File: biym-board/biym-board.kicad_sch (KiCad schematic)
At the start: 1 part

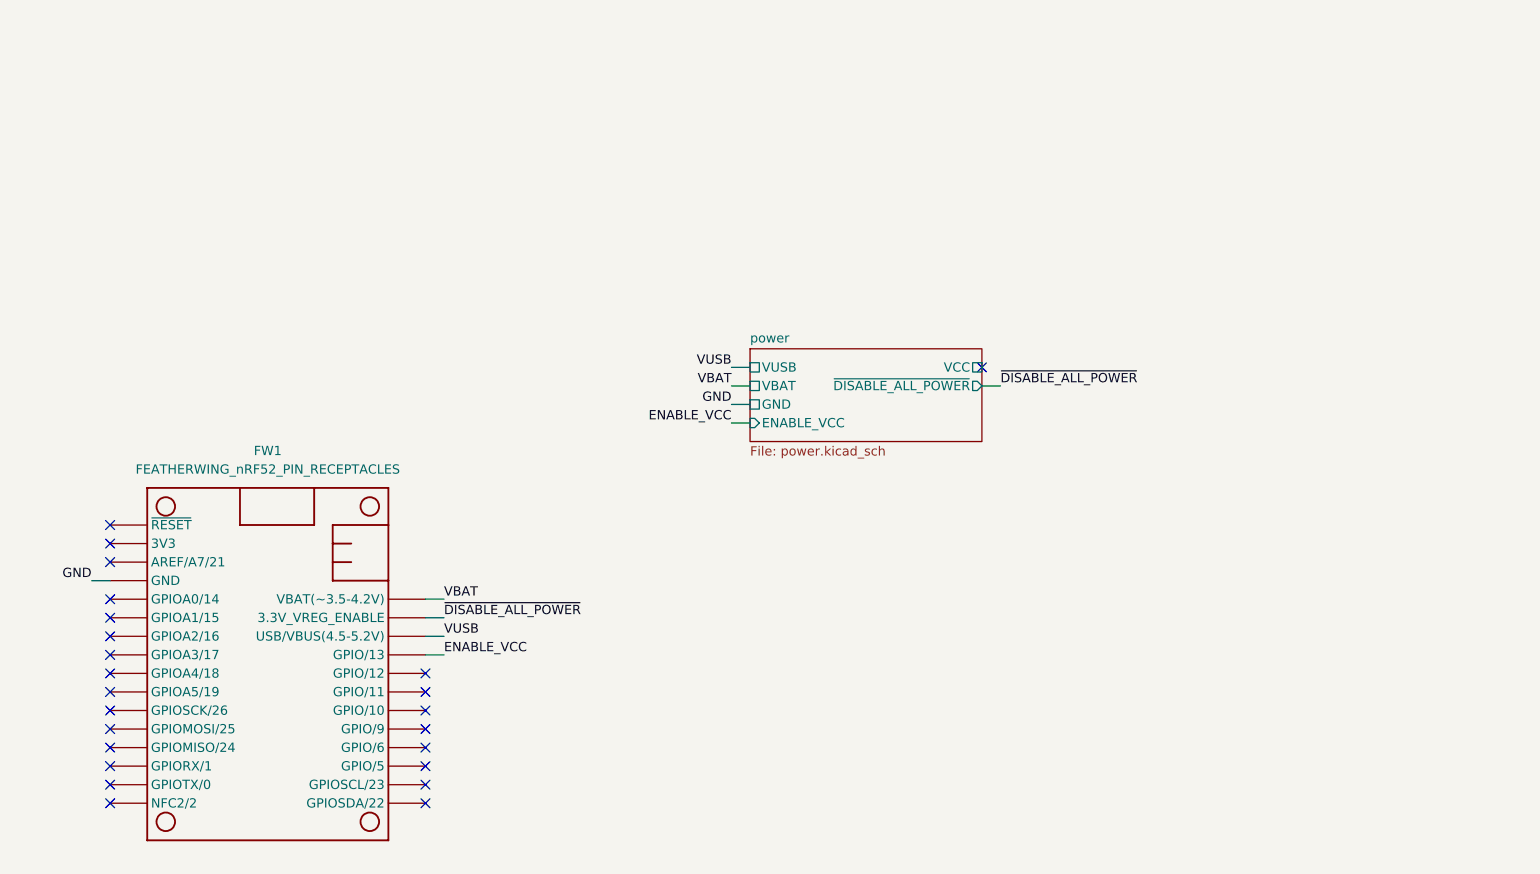
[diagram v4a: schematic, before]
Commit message: Switch feather contacts to pogo pins
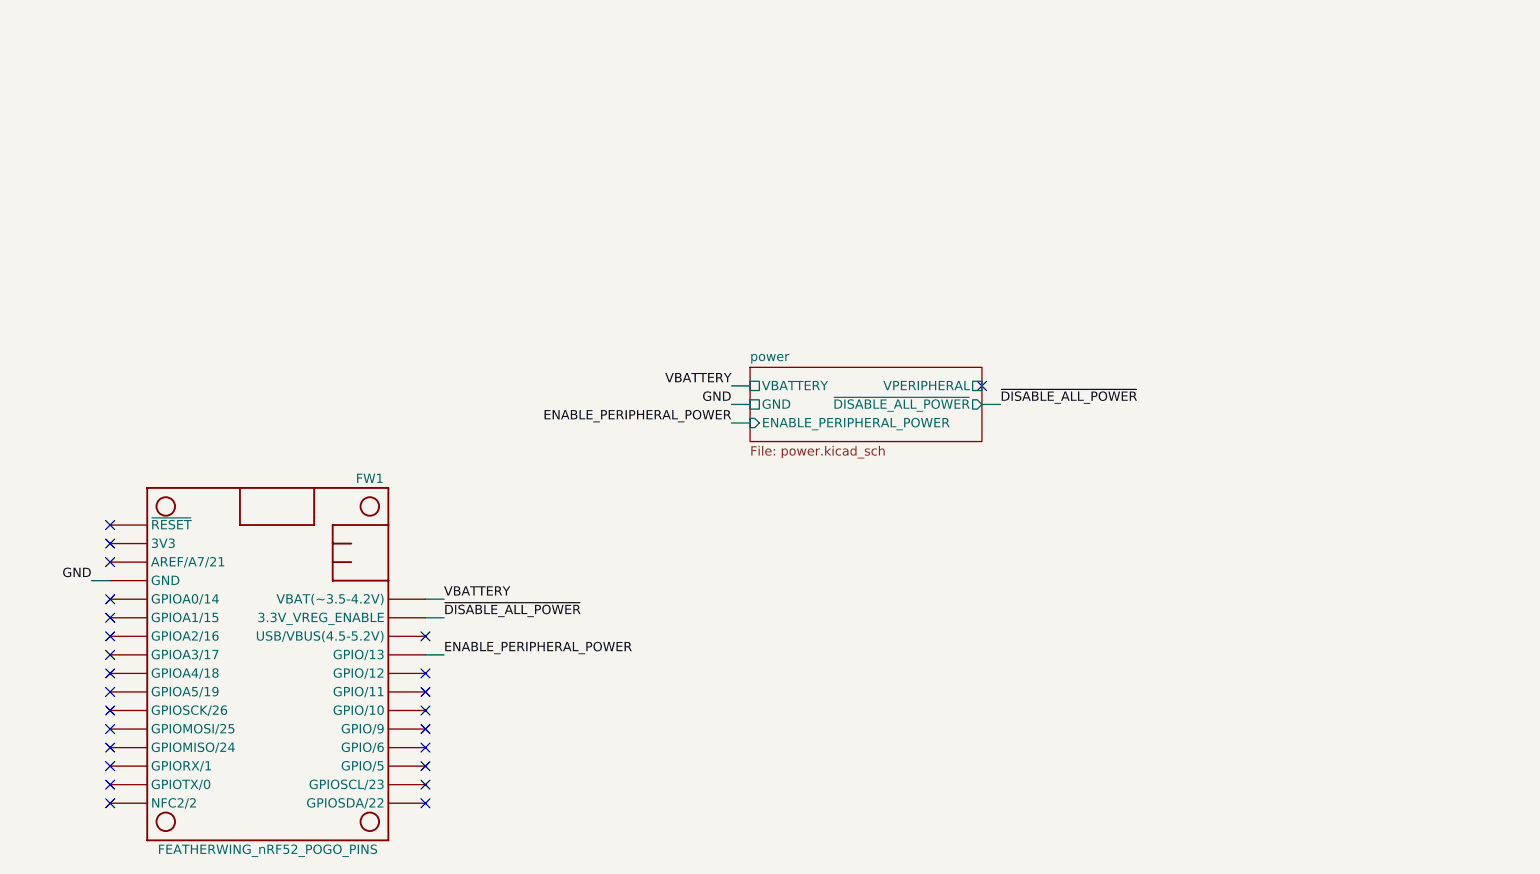
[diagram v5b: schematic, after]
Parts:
- removed FW1: FEATHERWING_nRF52_PIN_RECEPTACLES, Janelia:FEATHERWING_PIN_RECEPTACLES, symbol Janelia:FEATHERWING_nRF52_PIN_RECEPTACLES
- added FW1: FEATHERWING_nRF52_POGO_PINS, Janelia:FEATHERWING_POGO_PINS, symbol Janelia:FEATHERWING_nRF52_POGO_PINS
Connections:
- net GND: now also FW1.4 (GND)
- net ~{DISABLE_ALL_POWER}: now also FW1.27 (3.3V_VREG_ENABLE)
- new net ENABLE_PERIPHERAL_POWER: FW1.25 (GPIO/13)
- new net VBATTERY: FW1.28 (VBAT(~3.5-4.2V))
- no-connect marks 24 -> 25
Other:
- sheet power ports: added ENABLE_PERIPHERAL_POWER, VBATTERY, VPERIPHERAL; removed ENABLE_VCC, VBAT, VCC, VUSB
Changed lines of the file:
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@@
   (no_connect (at 49.53 110.49))
   (no_connect (at 92.71 115.57))
+  (no_connect (at 92.71 102.87))
   (no_connect (at 49.53 102.87))
   (no_connect (at 92.71 125.73))
   (no_connect (at 49.53 115.57))
   (no_connect (at 49.53 97.79))
-  (no_connect (at 168.91 66.04))
+  (no_connect (at 168.91 68.58))
   (no_connect (at 49.53 107.95))
   (no_connect (at 49.53 100.33))
@@
     (stroke (width 0) (type default) (color 0 0 0 0))
   )
-  (wire (pts (xy 168.91 68.58) (xy 171.45 68.58))
+  (wire (pts (xy 168.91 71.12) (xy 171.45 71.12))
     (stroke (width 0) (type default) (color 0 0 0 0))
   )
   (wire (pts (xy 46.99 95.25) (xy 49.53 95.25))
-    (stroke (width 0) (type default) (color 0 0 0 0))
-  )
-  (wire (pts (xy 92.71 102.87) (xy 95.25 102.87))
     (stroke (width 0) (type default) (color 0 0 0 0))
   )
@@
     (stroke (width 0) (type default) (color 0 0 0 0))
   )
-  (wire (pts (xy 137.16 66.04) (xy 134.62 66.04))
-    (stroke (width 0) (type default) (color 0 0 0 0))
-  )
-  (label "ENABLE_VCC" (at 95.25 105.41 0)
+  (label "ENABLE_PERIPHERAL_POWER" (at 95.25 105.41 0)
     (effects (font (size 1.27 1.27)) (justify left bottom))
   )
@@
     (effects (font (size 1.27 1.27)) (justify right bottom))
   )
-  (label "ENABLE_VCC" (at 134.62 73.66 180)
+  (label "ENABLE_PERIPHERAL_POWER" (at 134.62 73.66 180)
     (effects (font (size 1.27 1.27)) (justify right bottom))
   )
@@
     (effects (font (size 1.27 1.27)) (justify right bottom))
   )
-  (label "VBAT" (at 134.62 68.58 180)
+  (label "VBATTERY" (at 134.62 68.58 180)
     (effects (font (size 1.27 1.27)) (justify right bottom))
   )
-  (label "VUSB" (at 134.62 66.04 180)
-    (effects (font (size 1.27 1.27)) (justify right bottom))
-  )
-  (label "VUSB" (at 95.25 102.87 0)
-    (effects (font (size 1.27 1.27)) (justify left bottom))
-  )
-  (label "~{DISABLE_ALL_POWER}" (at 171.45 68.58 0)
+  (label "~{DISABLE_ALL_POWER}" (at 171.45 71.12 0)
     (effects (font (size 1.27 1.27)) (justify left bottom))
   )
@@
     (effects (font (size 1.27 1.27)) (justify left bottom))
   )
-  (label "VBAT" (at 95.25 97.79 0)
+  (label "VBATTERY" (at 95.25 97.79 0)
     (effects (font (size 1.27 1.27)) (justify left bottom))
   )
-  (symbol (lib_id "Janelia:FEATHERWING_nRF52_PIN_RECEPTACLES") (at 71.12 106.68 0) (unit 1)
-    (in_bom yes) (on_board yes) (fields_autoplaced)
-    (property "Reference" "FW1" (id 0) (at 71.12 77.47 0))
-    (property "Value" "FEATHERWING_nRF52_PIN_RECEPTACLES" (id 1) (at 71.12 80.01 0))
-    (property "Footprint" "Janelia:FEATHERWING_PIN_RECEPTACLES" (id 2) (at 71.12 72.39 0)
+  (symbol (lib_id "Janelia:FEATHERWING_nRF52_POGO_PINS") (at 71.12 106.68 0) (unit 1)
+    (in_bom yes) (on_board yes)
+    (property "Reference" "FW1" (id 0) (at 85.09 81.28 0))
+    (property "Value" "FEATHERWING_nRF52_POGO_PINS" (id 1) (at 71.12 132.08 0))
+    (property "Footprint" "Janelia:FEATHERWING_POGO_PINS" (id 2) (at 71.12 66.04 0)
       (effects (font (size 1.27 1.27)) hide)
     )
@@
       (effects (font (size 1.27 1.27)) hide)
     )
-    (property "Vendor" "Digi-Key" (id 4) (at 71.12 77.47 0)
+    (property "Vendor" "Digi-Key" (id 4) (at 71.12 76.2 0)
       (effects (font (size 1.524 1.524)) hide)
     )
-    (property "Vendor Part Number" "ED90331-ND" (id 5) (at 71.12 74.93 0)
+    (property "Vendor Part Number" "ED8110-04-ND" (id 5) (at 71.12 73.66 0)
       (effects (font (size 1.524 1.524)) hide)
     )
-    (property "Description" "CONN PIN RCPT .025-.037 SOLDER" (id 6) (at 71.12 72.39 0)
+    (property "Description" "CONN SPRING PISTON 4POS SMD" (id 6) (at 71.12 71.12 0)
       (effects (font (size 1.524 1.524)) hide)
     )
-    (property "Quantity" "28" (id 7) (at 71.12 106.68 0)
+    (property "Quantity" "7" (id 7) (at 71.12 63.5 0)
       (effects (font (size 1.27 1.27)) hide)
     )
-    (property "Manufacturer" "Mill-Max Manufacturing Corp." (id 8) (at 71.12 106.68 0)
+    (property "Manufacturer" "Mill-Max Manufacturing Corp." (id 8) (at 71.12 60.96 0)
       (effects (font (size 1.27 1.27)) hide)
     )
-    (property "Manufacturer Part Number" "0305-0-15-15-47-27-10-0" (id 9) (at 71.12 106.68 0)
+    (property "Manufacturer Part Number" "811-22-004-30-000101" (id 9) (at 71.12 68.58 0)
       (effects (font (size 1.27 1.27)) hide)
     )
@@
     (pin "9")
   )
-  (sheet (at 137.16 63.5) (size 31.75 12.7) (fields_autoplaced)
+  (sheet (at 137.16 66.04) (size 31.75 10.16) (fields_autoplaced)
     (stroke (width 0.1524) (type solid) (color 0 0 0 0))
     (fill (color 0 0 0 0.0000))
-    (property "Sheet name" "power" (id 0) (at 137.16 62.7884 0)
+    (property "Sheet name" "power" (id 0) (at 137.16 65.3284 0)
       (effects (font (size 1.27 1.27)) (justify left bottom))
     )
@@
       (effects (font (size 1.27 1.27)) (justify left))
     )
-    (pin "VCC" passive (at 168.91 66.04 0)
+    (pin "VPERIPHERAL" passive (at 168.91 68.58 0)
       (effects (font (size 1.27 1.27)) (justify right))
     )
-    (pin "VBAT" passive (at 137.16 68.58 180)
+    (pin "VBATTERY" passive (at 137.16 68.58 180)
       (effects (font (size 1.27 1.27)) (justify left))
     )
-    (pin "VUSB" passive (at 137.16 66.04 180)
-      (effects (font (size 1.27 1.27)) (justify left))
-    )
-    (pin "~{DISABLE_ALL_POWER}" output (at 168.91 68.58 0)
+    (pin "~{DISABLE_ALL_POWER}" output (at 168.91 71.12 0)
       (effects (font (size 1.27 1.27)) (justify right))
     )
-    (pin "ENABLE_VCC" input (at 137.16 73.66 180)
+    (pin "ENABLE_PERIPHERAL_POWER" input (at 137.16 73.66 180)
       (effects (font (size 1.27 1.27)) (justify left))
     )
@@
   )
   (symbol_instances
-    (path "/2c398cb1-cb17-49ba-86d6-22731656ead9/ae7d77aa-4639-4a04-8768-f2282fb5051c"
-      (reference "D1") (unit 1) (value "DIODE_SCHOTTKY_40V_2A_0603") (footprint "Janelia:SM0603_DSN2")
-    )
-    (path "/2c398cb1-cb17-49ba-86d6-22731656ead9/7ddeef5d-5855-4b75-a2bc-b5412afa8482"
-      (reference "D2") (unit 1) (value "DIODE_SCHOTTKY_40V_2A_0603") (footprint "Janelia:SM0603_DSN2")
-    )
-    (path "/55a2d7cd-47d7-49c1-94ac-5e60fd064dcf"
-      (reference "FW1") (unit 1) (value "FEATHERWING_nRF52_PIN_RECEPTACLES") (footprint "Janelia:FEATHERWING_PIN_RECEPTACLES")
+    (path "/78609776-14fe-41ec-972c-2bdc49eac818"
+      (reference "FW1") (unit 1) (value "FEATHERWING_nRF52_POGO_PINS") (footprint "Janelia:FEATHERWING_POGO_PINS")
     )
     (path "/2c398cb1-cb17-49ba-86d6-22731656ead9/ee181020-0a66-4e94-8afa-04e718523ff4"

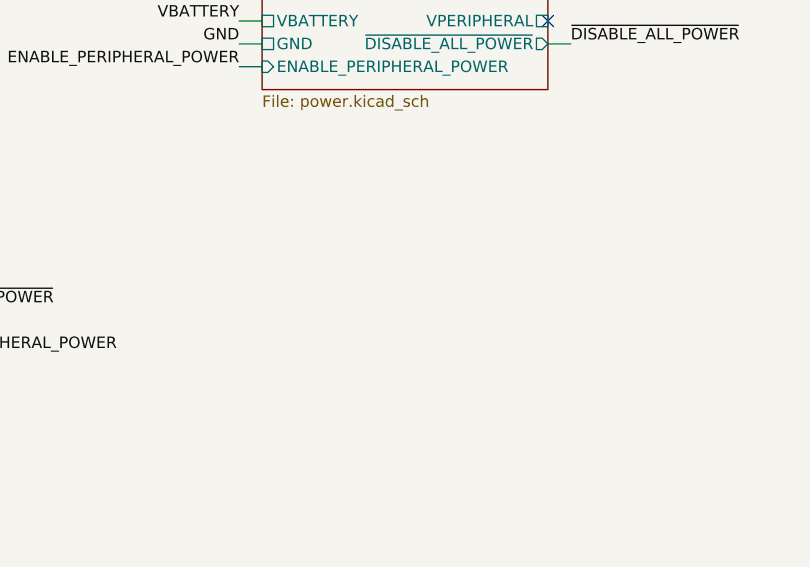
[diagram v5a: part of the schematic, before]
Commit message: Add motor sheet
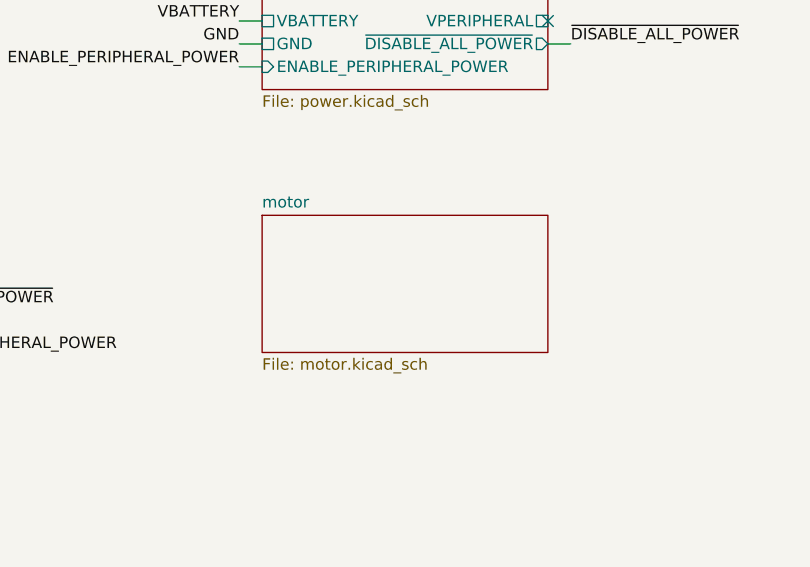
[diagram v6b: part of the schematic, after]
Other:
- added sheet motor (motor.kicad_sch)
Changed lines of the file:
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@@
   (title_block
     (title "biym-board")
-    (date "2022-11-10")
+    (date "2022-11-11")
     (rev "0.1")
     (company "Peter Polidoro")
@@
     )
   )
+  (sheet (at 137.16 90.17) (size 31.75 15.24) (fields_autoplaced)
+    (stroke (width 0.1524) (type solid) (color 0 0 0 0))
+    (fill (color 0 0 0 0.0000))
+    (property "Sheet name" "motor" (id 0) (at 137.16 89.4584 0)
+      (effects (font (size 1.27 1.27)) (justify left bottom))
+    )
+    (property "Sheet file" "motor.kicad_sch" (id 1) (at 137.16 105.9946 0)
+      (effects (font (size 1.27 1.27)) (justify left top))
+    )
+  )
   (sheet_instances
     (path "/" (page "1"))
     (path "/2c398cb1-cb17-49ba-86d6-22731656ead9" (page "2"))
+    (path "/79116d11-26fd-48fc-b8f9-7a7b774125a1" (page "3"))
   )
   (symbol_instances
